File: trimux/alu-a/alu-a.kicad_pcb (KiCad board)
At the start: 2 copper layers, 150 x 100 mm, 0 parts

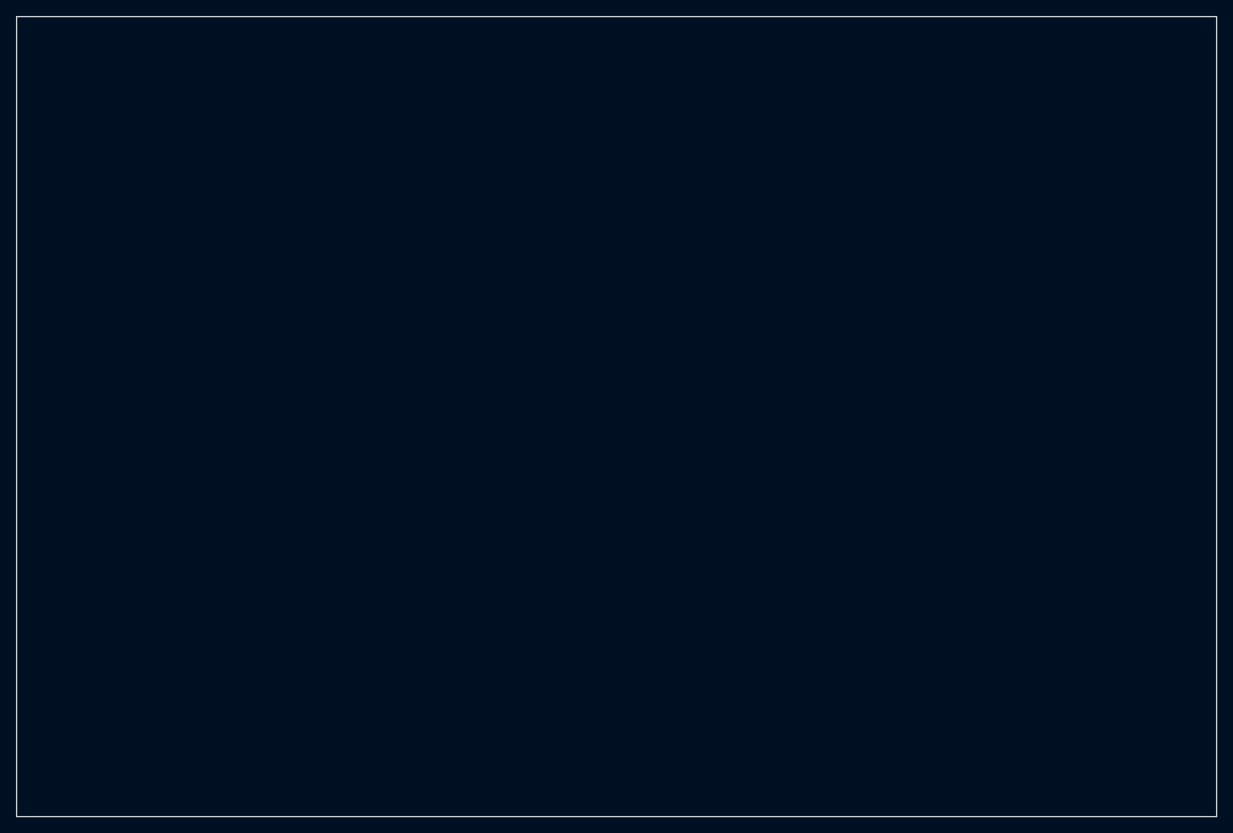
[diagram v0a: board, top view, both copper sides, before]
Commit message: alu-a routed
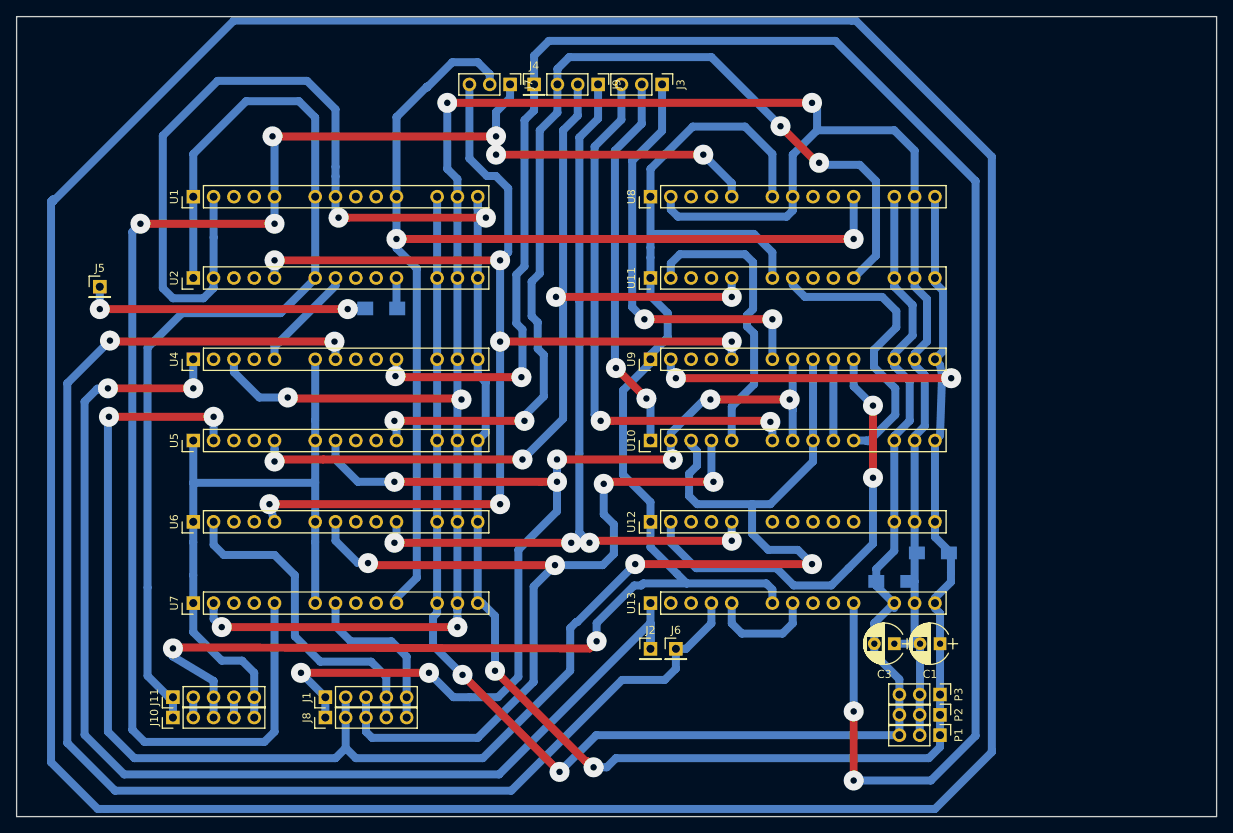
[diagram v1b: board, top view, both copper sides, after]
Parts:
- added C1: 4.7u, Capacitors_THT:CP_Radial_D5.0mm_P2.50mm, F.Cu at (130.4, 93.4)
- added C2: .1u, Capacitors_SMD:C_1206_HandSoldering, B.Cu at (129.5, 82.0)
- added C3: 4.7u, Capacitors_THT:CP_Radial_D5.0mm_P2.50mm, F.Cu at (124.7, 93.4)
- added C4: .1u, Capacitors_SMD:C_1206_HandSoldering, B.Cu at (124.5, 85.6)
- added J1: Conn_01x05, Pin_Headers:Pin_Header_Straight_1x05_Pitch2.54mm, F.Cu at (53.6, 100.1)
- added J10: Conn_01x05, Pin_Headers:Pin_Header_Straight_1x05_Pitch2.54mm, F.Cu at (34.5, 102.6)
- added J11: Conn_01x05, Pin_Headers:Pin_Header_Straight_1x05_Pitch2.54mm, F.Cu at (34.5, 100.1)
- added J2: Conn_01x01, Pin_Headers:Pin_Header_Straight_1x01_Pitch2.54mm, F.Cu at (94.2, 94.0)
- added J3: Conn_01x03, Pin_Headers:Pin_Header_Straight_1x03_Pitch2.54mm, F.Cu at (95.7, 23.5)
- added J4: Conn_01x01, Pin_Headers:Pin_Header_Straight_1x01_Pitch2.54mm, F.Cu at (79.7, 23.5)
- added J5: Conn_01x01, Pin_Headers:Pin_Header_Straight_1x01_Pitch2.54mm, F.Cu at (25.4, 48.8)
- added J6: Conn_01x01, Pin_Headers:Pin_Header_Straight_1x01_Pitch2.54mm, F.Cu at (97.4, 94.0)
- added J7: Conn_01x03, Pin_Headers:Pin_Header_Straight_1x03_Pitch2.54mm, F.Cu at (76.7, 23.5)
- added J8: Conn_01x05, Pin_Headers:Pin_Header_Straight_1x05_Pitch2.54mm, F.Cu at (53.6, 102.6)
- added J9: Conn_01x03, Pin_Headers:Pin_Header_Straight_1x03_Pitch2.54mm, F.Cu at (87.7, 23.5)
- added P1: CONN_01X03, Pin_Headers:Pin_Header_Straight_1x03_Pitch2.54mm, F.Cu at (130.4, 104.8)
- added P2: CONN_01X03, Pin_Headers:Pin_Header_Straight_1x03_Pitch2.54mm, F.Cu at (130.4, 102.3)
- added P3: CONN_01X03, Pin_Headers:Pin_Header_Straight_1x03_Pitch2.54mm, F.Cu at (130.4, 99.7)
- added R1: 10k, Resistors_SMD:R_1206_HandSoldering, B.Cu at (60.6, 51.5)
- added U1: trimux, trimux:trimux1x15_2.54, F.Cu at (37.1, 37.5)
- added U10: trimux, trimux:trimux1x15_2.54, F.Cu at (94.2, 68.0)
- added U11: trimux, trimux:trimux1x15_2.54, F.Cu at (94.2, 47.7)
- added U12: trimux, trimux:trimux1x15_2.54, F.Cu at (94.2, 78.2)
- added U13: trimux, trimux:trimux1x15_2.54, F.Cu at (94.2, 88.3)
- added U2: trimux, trimux:trimux1x15_2.54, F.Cu at (37.1, 47.7)
- added U4: trimux, trimux:trimux1x15_2.54, F.Cu at (37.1, 57.8)
- added U5: trimux, trimux:trimux1x15_2.54, F.Cu at (37.1, 68.0)
- added U6: trimux, trimux:trimux1x15_2.54, F.Cu at (37.1, 78.2)
- added U7: trimux, trimux:trimux1x15_2.54, F.Cu at (37.1, 88.3)
- added U8: trimux, trimux:trimux1x15_2.54, F.Cu at (94.2, 37.5)
- added U9: trimux, trimux:trimux1x15_2.54, F.Cu at (94.2, 57.8)
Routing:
- net (no net): track 0.00 -> 401.9 mm
- net +5V: track 0.00 -> 332.3 mm, vias 0 -> 6
- net GNDREF: track 0.00 -> 303.6 mm, vias 0 -> 6
- net /MEM_CLK: track 0.00 -> 231.8 mm, vias 0 -> 4
- net /OPCODE_1: track 0.00 -> 216.7 mm, vias 0 -> 4
- net -5V: track 0.00 -> 198.8 mm, vias 0 -> 2
- net /MEM_HI: track 0.00 -> 196.6 mm, vias 0 -> 6
- net /ENABLE_OPA: track 0.00 -> 195.4 mm, vias 0 -> 2
- net /COUNTER_CLOCK: track 0.00 -> 178.5 mm, vias 0 -> 2
- net /INSTRUCTION_CYCLE: track 0.00 -> 149.3 mm, vias 0 -> 2
- net /MEM_LO: track 0.00 -> 148.2 mm, vias 0 -> 6
- net /MEM_MI: track 0.00 -> 142.9 mm, vias 0 -> 2
- net /OPCODE_0: track 0.00 -> 142.4 mm, vias 0 -> 8
- net /ENABLE_JMP: track 0.00 -> 126.8 mm
- net /MEM_A_LO: track 0.00 -> 125.9 mm, vias 0 -> 4
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
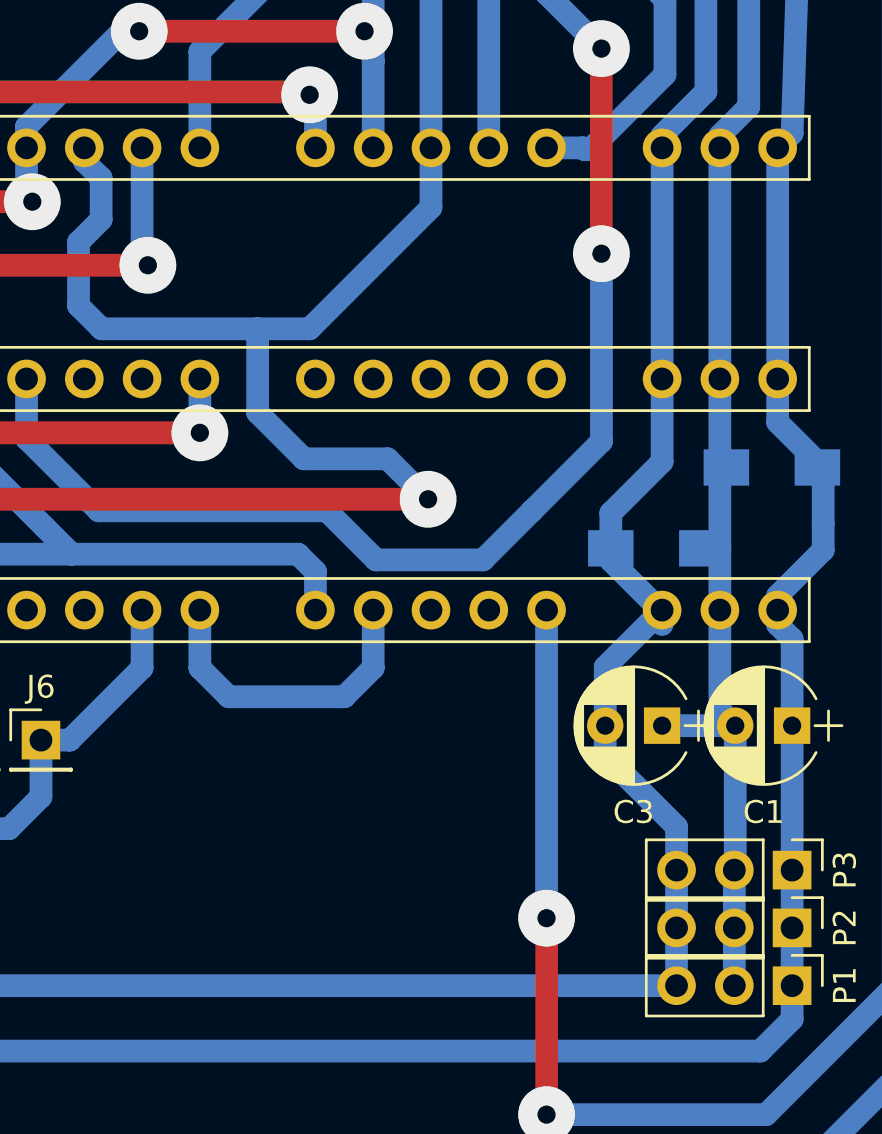
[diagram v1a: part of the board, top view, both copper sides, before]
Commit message: opselector rerouted
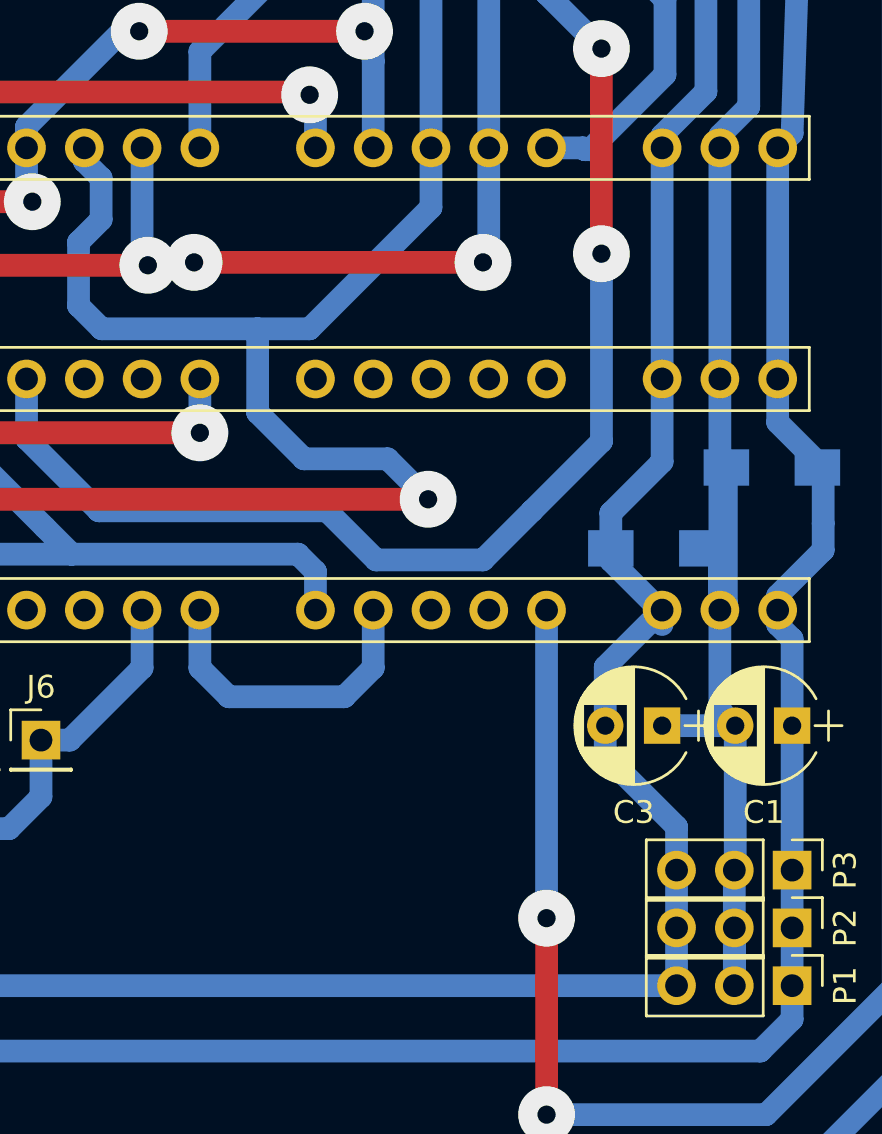
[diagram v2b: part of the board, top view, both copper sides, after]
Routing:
- net /OPCODE_2: track 121.7 -> 141.7 mm, vias 4 -> 6
- net GNDREF: track 303.6 -> 315.2 mm
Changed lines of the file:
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@@
   (general
     (links 131)
-    (no_connects 4)
+    (no_connects 0)
     (area 14.924999 14.924999 165.075001 115.075001)
     (thickness 1.6)
     (drawings 4)
-    (tracks 657)
+    (tracks 668)
     (zones 0)
     (modules 31)
@@
   (segment (start 72.644 47.671) (end 72.644 37.511) (width 1) (layer B.Cu) (net 1))
   (segment (start 72.644 78.151) (end 72.644 67.991) (width 1) (layer B.Cu) (net 1))
+  (segment (start 127.889 102.281) (end 127.889 104.821) (width 1) (layer B.Cu) (net 2))
+  (segment (start 127.54 82.042) (end 127.54 88.025) (width 1) (layer B.Cu) (net 2))
+  (segment (start 127.54 88.025) (end 127.254 88.311) (width 1) (layer B.Cu) (net 2))
+  (segment (start 126.46 85.598) (end 127.254 85.598) (width 1) (layer B.Cu) (net 2))
+  (segment (start 127.254 85.598) (end 127.254 88.311) (width 1) (layer B.Cu) (net 2))
   (segment (start 70.104 37.511) (end 70.104 35.306) (width 1) (layer B.Cu) (net 2))
   (segment (start 115.062 26.416) (end 115.062 29.21) (width 1) (layer B.Cu) (net 2))
@@
   (segment (start 39.624 88.311) (end 39.624 89.027) (width 1) (layer B.Cu) (net 2))
   (segment (start 70.104 89.154) (end 70.104 88.311) (width 1) (layer B.Cu) (net 2))
-  (segment (start 126.46 85.598) (end 127.254 85.598) (width 1) (layer B.Cu) (net 2))
   (segment (start 70.104 62.738) (end 70.485 62.738) (width 1) (layer B.Cu) (net 2))
   (segment (start 70.485 62.738) (end 70.612 62.865) (width 1) (layer B.Cu) (net 2))
@@
   (segment (start 99.314 68.58) (end 99.314 67.991) (width 1) (layer B.Cu) (net 5))
   (segment (start 114.554 67.991) (end 114.554 57.831) (width 1) (layer B.Cu) (net 5))
+  (segment (start 117.094 67.991) (end 117.094 72.771) (width 1) (layer B.Cu) (net 6))
+  (segment (start 104.013 73.152) (end 102.108 73.152) (width 1) (layer B.Cu) (net 6))
+  (segment (start 104.14 73.025) (end 104.013 73.152) (width 1) (layer B.Cu) (net 6))
+  (via (at 104.14 73.025) (size 2.5) (drill 0.8) (layers F.Cu B.Cu) (net 6))
+  (segment (start 116.84 73.025) (end 104.14 73.025) (width 1) (layer F.Cu) (net 6))
+  (via (at 116.84 73.025) (size 2.5) (drill 0.8) (layers F.Cu B.Cu) (net 6))
+  (segment (start 117.094 72.771) (end 116.84 73.025) (width 1) (layer B.Cu) (net 6))
   (segment (start 58.674 102.616) (end 58.674 104.394) (width 1) (layer B.Cu) (net 6))
   (segment (start 79.629 86.233) (end 82.296 83.566) (width 1) (layer B.Cu) (net 6))
@@
   (segment (start 58.674 100.076) (end 58.674 102.616) (width 1) (layer B.Cu) (net 6))
   (segment (start 89.662 81.915) (end 89.662 82.169) (width 1) (layer B.Cu) (net 6))
+  (segment (start 89.662 82.169) (end 88.265 83.566) (width 1) (layer B.Cu) (net 6))
+  (segment (start 82.296 83.566) (end 88.265 83.566) (width 1) (layer B.Cu) (net 6))
+  (segment (start 89.662 81.915) (end 89.662 78.486) (width 1) (layer B.Cu) (net 6))
+  (segment (start 89.662 78.486) (end 88.392 77.216) (width 1) (layer B.Cu) (net 6))
+  (segment (start 88.392 77.216) (end 88.392 73.406) (width 1) (layer B.Cu) (net 6))
+  (via (at 88.392 73.406) (size 2.5) (drill 0.8) (layers F.Cu B.Cu) (net 6))
+  (segment (start 88.392 73.406) (end 88.646 73.152) (width 1) (layer F.Cu) (net 6))
+  (segment (start 88.646 73.152) (end 102.108 73.152) (width 1) (layer F.Cu) (net 6))
+  (via (at 102.108 73.152) (size 2.5) (drill 0.8) (layers F.Cu B.Cu) (net 6))
   (segment (start 101.854 72.898) (end 101.854 67.991) (width 1) (layer B.Cu) (net 6))
   (segment (start 102.108 73.152) (end 101.854 72.898) (width 1) (layer B.Cu) (net 6))
-  (via (at 102.108 73.152) (size 2.5) (drill 0.8) (layers F.Cu B.Cu) (net 6))
-  (segment (start 88.646 73.152) (end 102.108 73.152) (width 1) (layer F.Cu) (net 6))
-  (segment (start 88.392 73.406) (end 88.646 73.152) (width 1) (layer F.Cu) (net 6))
-  (via (at 88.392 73.406) (size 2.5) (drill 0.8) (layers F.Cu B.Cu) (net 6))
-  (segment (start 88.392 77.216) (end 88.392 73.406) (width 1) (layer B.Cu) (net 6))
-  (segment (start 89.662 78.486) (end 88.392 77.216) (width 1) (layer B.Cu) (net 6))
-  (segment (start 89.662 81.915) (end 89.662 78.486) (width 1) (layer B.Cu) (net 6))
-  (segment (start 82.296 83.566) (end 88.265 83.566) (width 1) (layer B.Cu) (net 6))
-  (segment (start 89.662 82.169) (end 88.265 83.566) (width 1) (layer B.Cu) (net 6))
   (via (at 82.296 83.566) (size 2.5) (drill 0.8) (layers F.Cu B.Cu) (net 6))
   (segment (start 54.864 78.151) (end 54.864 80.518) (width 1) (layer B.Cu) (net 6))
